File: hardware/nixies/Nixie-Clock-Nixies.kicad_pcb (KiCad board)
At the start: 2 copper layers, 228.6 x 52.1 mm, 25 parts, among them J1 Nixies-Connector

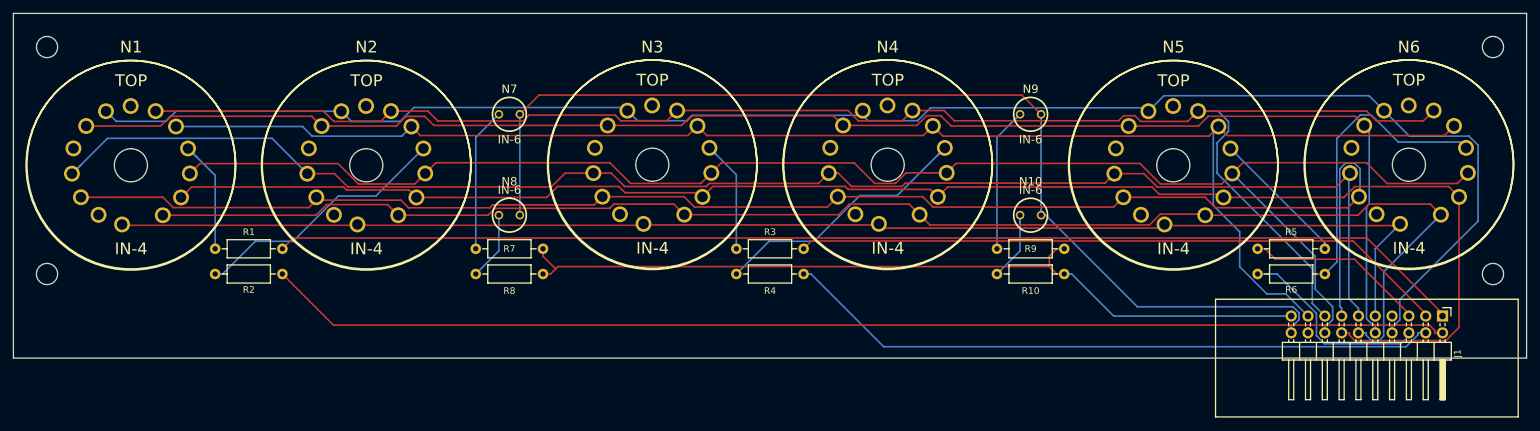
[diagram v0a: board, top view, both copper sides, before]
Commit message: Fix nixie drill hole size
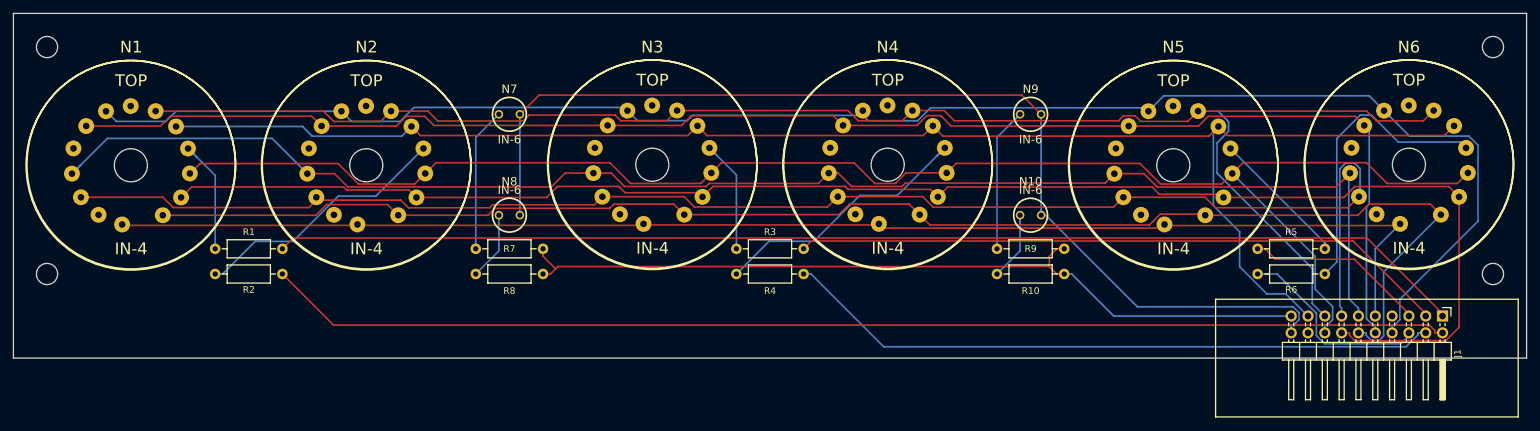
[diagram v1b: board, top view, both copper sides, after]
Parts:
- N1, N2, N3, N4, N5, N6: footprint nixies-us:nixies-us-IN-4-DSUB -> nixie-clock:nixies-us-IN-4-DSUB_edited

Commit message: Move to Kicad 6
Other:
- net class Default removed
